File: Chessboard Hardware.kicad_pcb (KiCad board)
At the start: 2 copper layers, 200 x 200 mm, 86 parts, among them J1 Conn_01x04_Pin

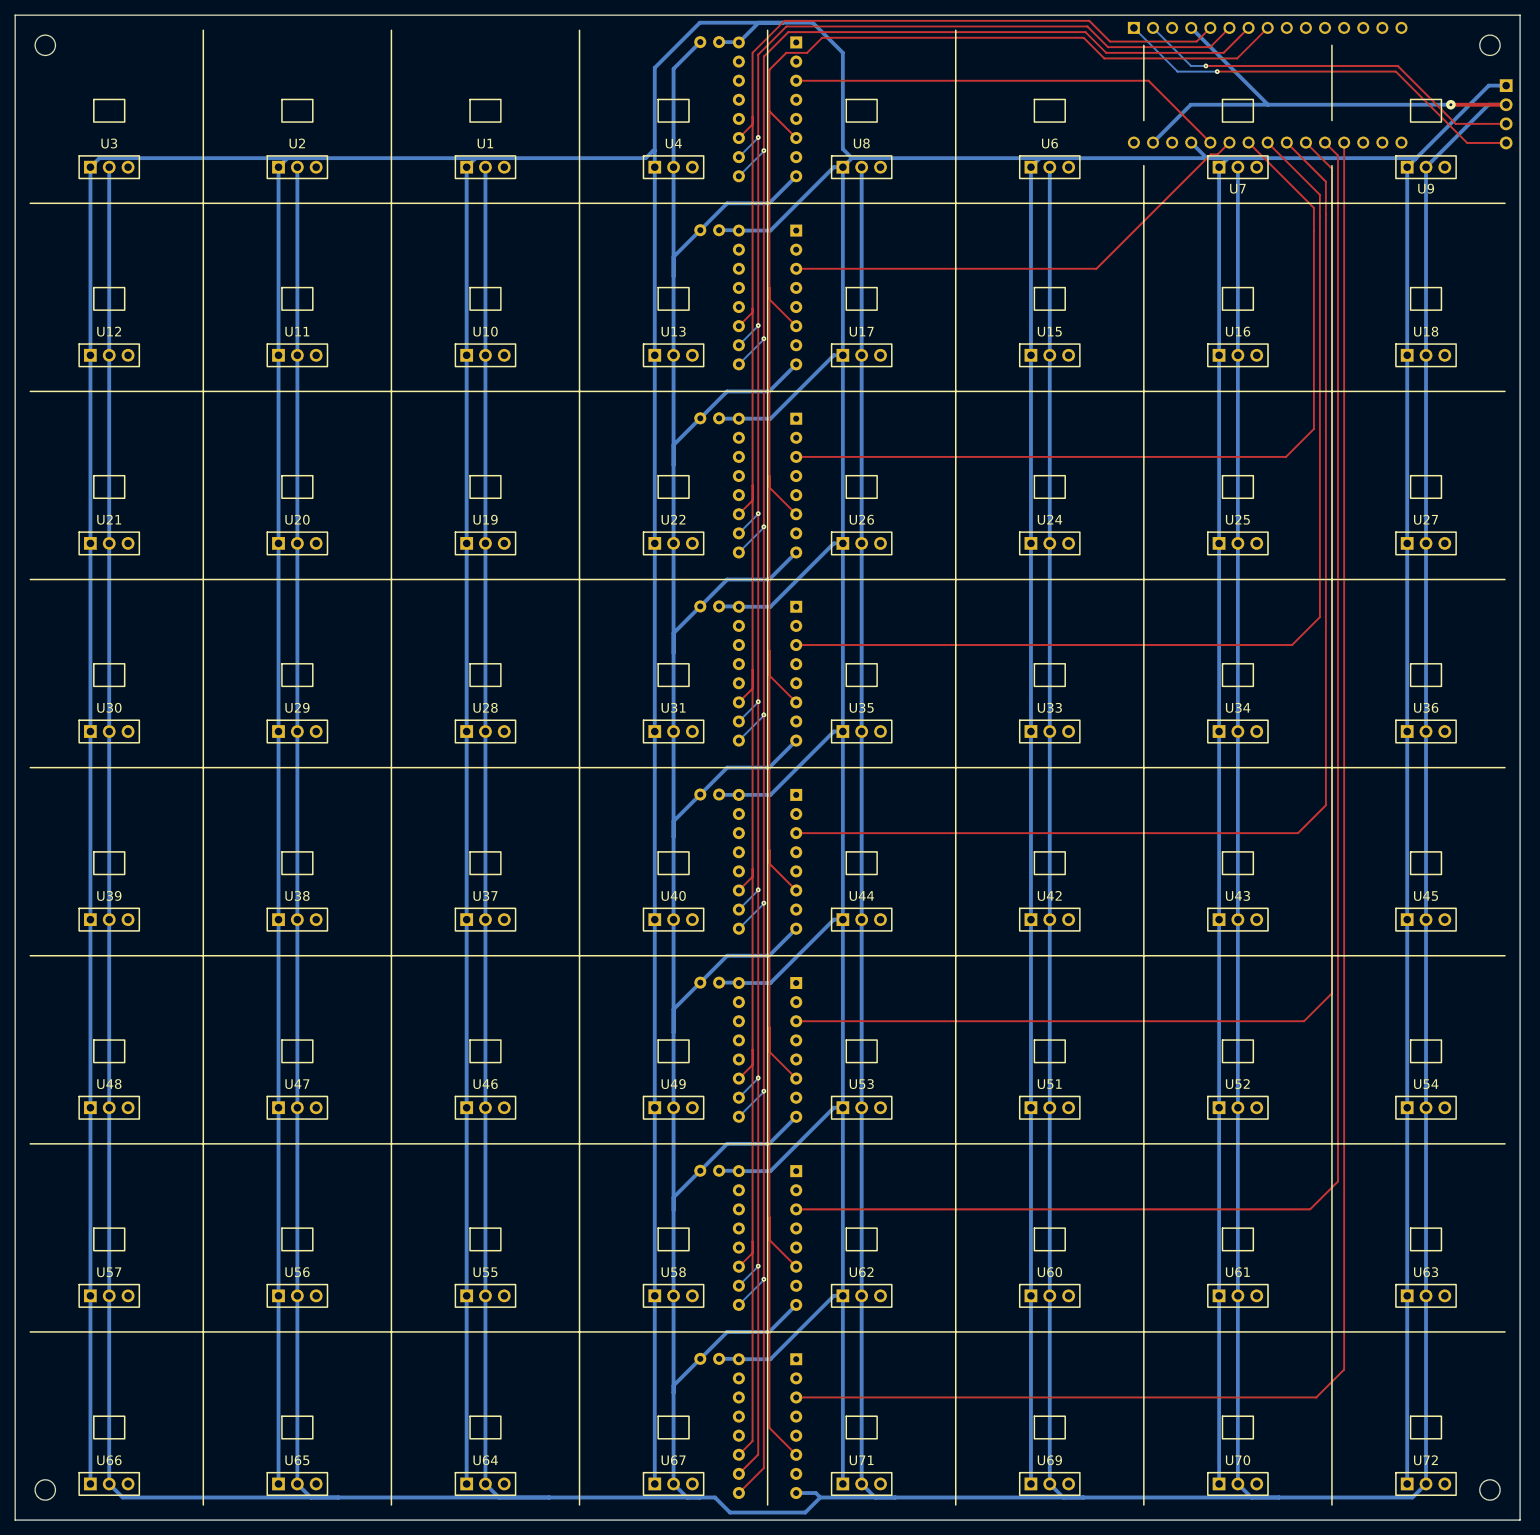
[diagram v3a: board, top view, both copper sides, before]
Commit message: Route left side linear halls
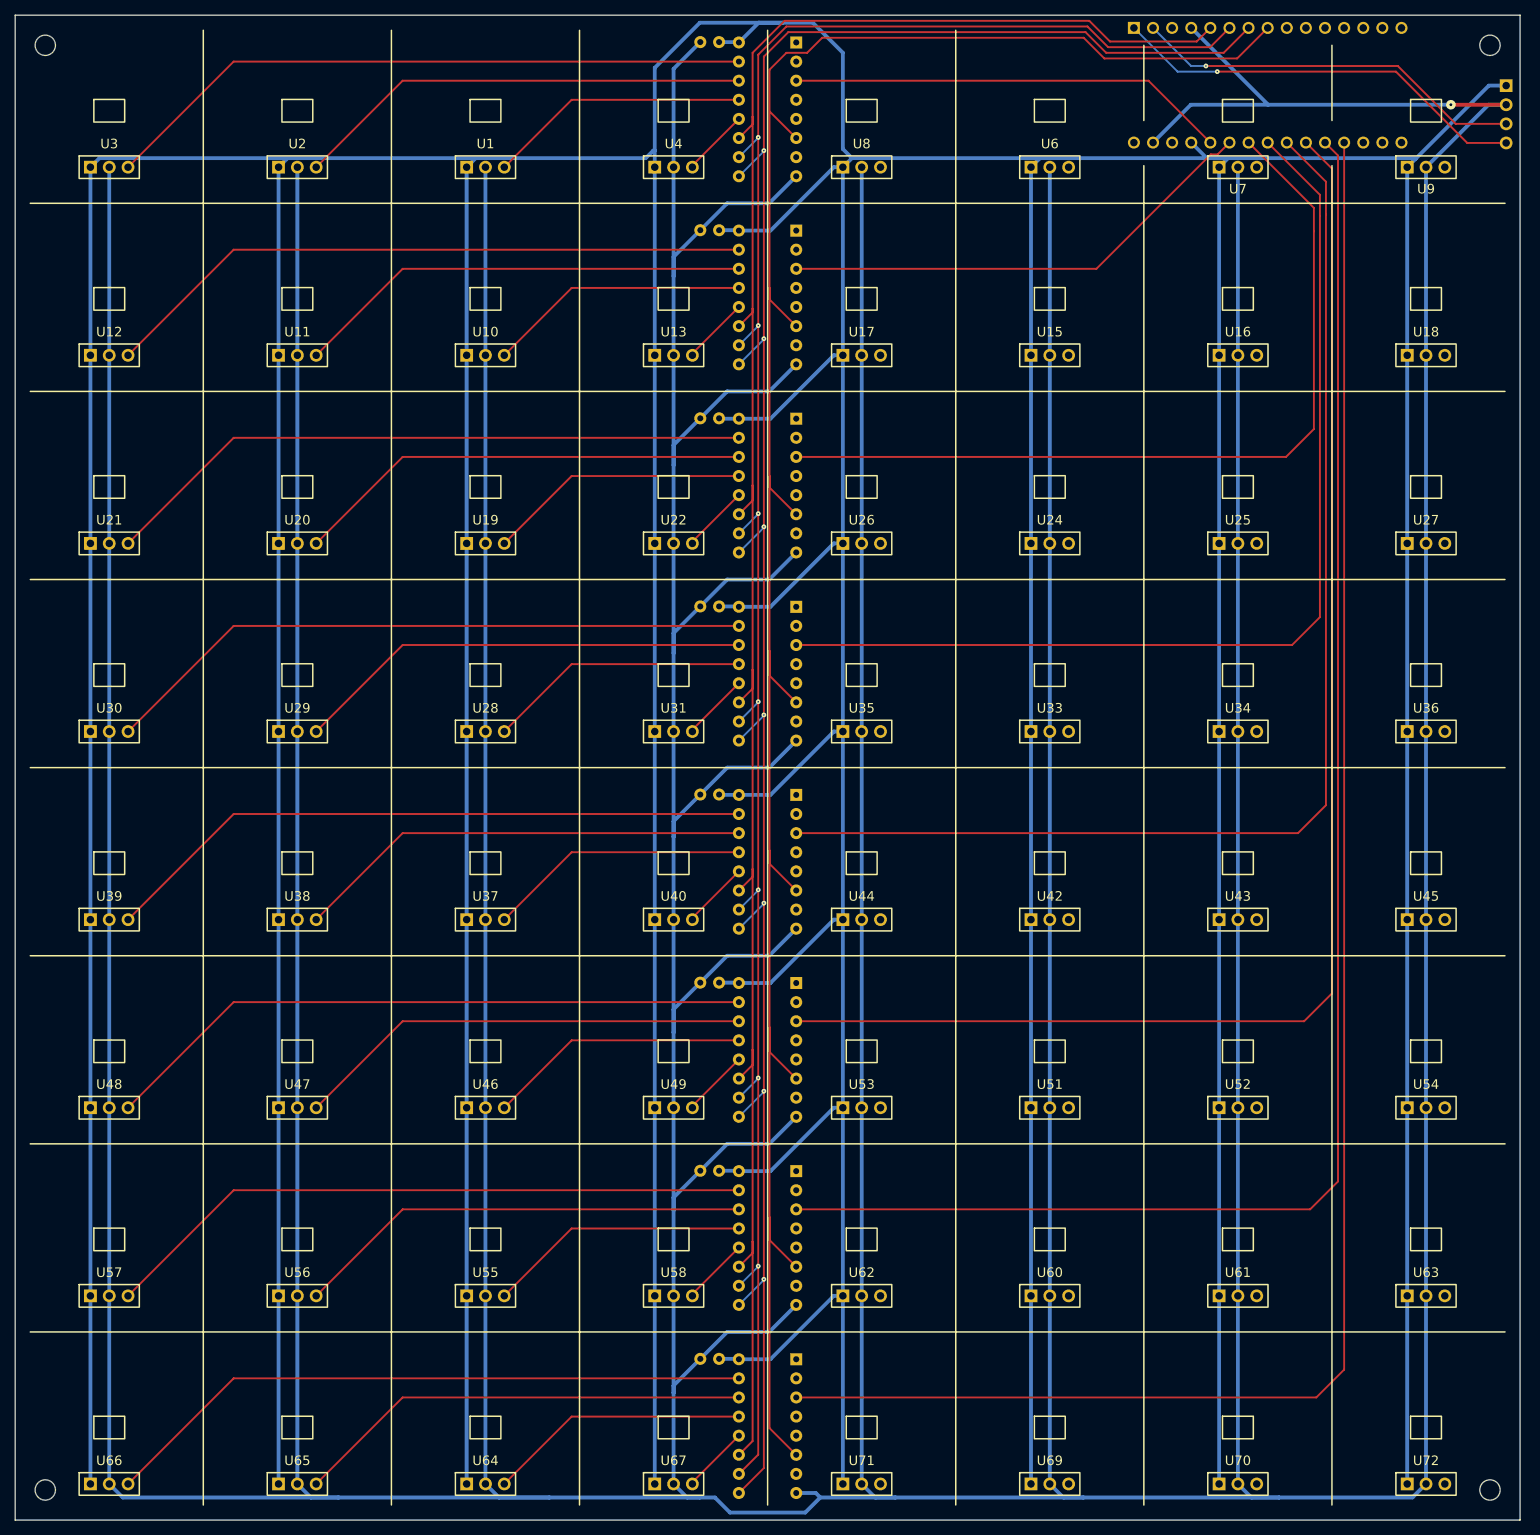
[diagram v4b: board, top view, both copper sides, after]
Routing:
- net Net-(U66-SIG): track 0.00 -> 87.0 mm
- net Net-(U57-SIG): track 0.00 -> 87.0 mm
- net Net-(U48-SIG): track 0.00 -> 87.0 mm
- net Net-(U39-SIG): track 0.00 -> 87.0 mm
- net Net-(U30-SIG): track 0.00 -> 87.0 mm
- net Net-(U3-SIG): track 0.00 -> 87.0 mm
- net Net-(U21-SIG): track 0.00 -> 87.0 mm
- net Net-(U12-SIG): track 0.00 -> 87.0 mm
- net Net-(U20-SIG): track 0.00 -> 60.9 mm
- net Net-(U2-SIG): track 0.00 -> 60.9 mm
- net Net-(U11-SIG): track 0.00 -> 60.9 mm
- net Net-(U65-SIG): track 0.00 -> 60.9 mm
- net Net-(U56-SIG): track 0.00 -> 60.9 mm
- net Net-(U47-SIG): track 0.00 -> 60.9 mm
- net Net-(U38-SIG): track 0.00 -> 60.9 mm
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
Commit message: Finish routing linear halls
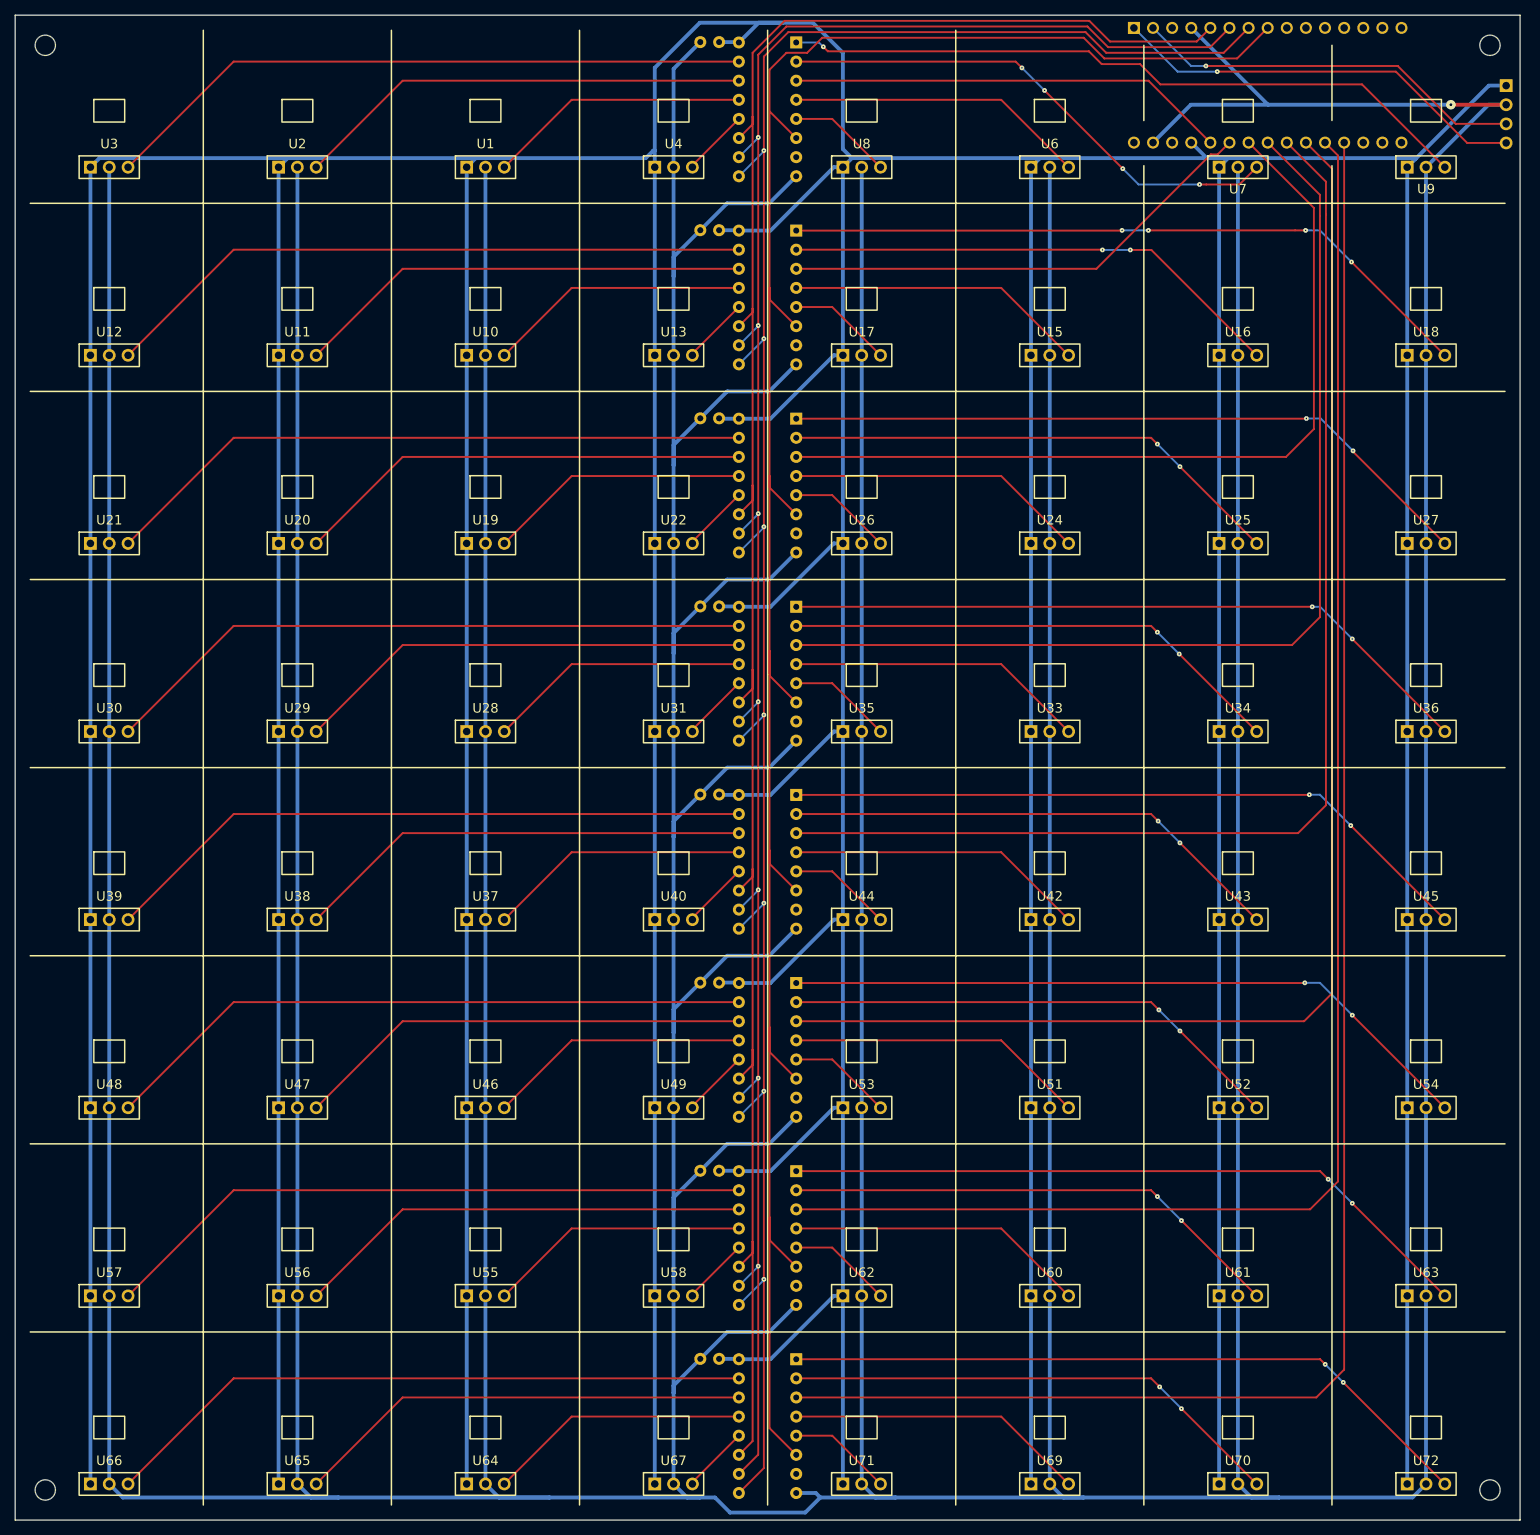
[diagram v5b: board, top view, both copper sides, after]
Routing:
- net Net-(U23-Y4): track 0.00 -> 93.1 mm, vias 0 -> 2
- net Net-(U32-Y4): track 0.00 -> 93.1 mm, vias 0 -> 2
- net Net-(U14-Y4): track 0.00 -> 93.1 mm, vias 0 -> 4
- net Net-(U41-Y4): track 0.00 -> 93.1 mm, vias 0 -> 2
- net Net-(U50-Y4): track 0.00 -> 93.1 mm, vias 0 -> 2
- net Net-(U5-Y4): track 0.00 -> 93.1 mm, vias 0 -> 1
- net Net-(U68-Y4): track 0.00 -> 93.1 mm, vias 0 -> 2
- net Net-(U59-Y4): track 0.00 -> 93.1 mm, vias 0 -> 2
- net Net-(U5-Y6): track 0.00 -> 68.9 mm, vias 0 -> 4
- net Net-(U68-Y6): track 0.00 -> 67.0 mm, vias 0 -> 2
- net Net-(U59-Y6): track 0.00 -> 67.0 mm, vias 0 -> 2
- net Net-(U50-Y6): track 0.00 -> 67.0 mm, vias 0 -> 2
- net Net-(U41-Y6): track 0.00 -> 67.0 mm, vias 0 -> 2
- net Net-(U32-Y6): track 0.00 -> 67.0 mm, vias 0 -> 2
- net Net-(U23-Y6): track 0.00 -> 67.0 mm, vias 0 -> 2
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
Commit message: Finish test pad routing
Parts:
- added TP1: TestPoint, Connector_PinHeader_2.54mm:PinHeader_1x01_P2.54mm_Vertical, B.Cu at (240.0, 78.3)
- added TP10: TestPoint, Connector_PinHeader_2.54mm:PinHeader_1x01_P2.54mm_Vertical, B.Cu at (221.0, 137.0)
- added TP11: TestPoint, Connector_PinHeader_2.54mm:PinHeader_1x01_P2.54mm_Vertical, B.Cu at (221.0, 162.0)
- added TP12: TestPoint, Connector_PinHeader_2.54mm:PinHeader_1x01_P2.54mm_Vertical, B.Cu at (221.0, 187.0)
- added TP13: TestPoint, Connector_PinHeader_2.54mm:PinHeader_1x01_P2.54mm_Vertical, B.Cu at (221.0, 212.0)
- added TP14: TestPoint, Connector_PinHeader_2.54mm:PinHeader_1x01_P2.54mm_Vertical, B.Cu at (221.0, 237.0)
- added TP2: TestPoint, Connector_PinHeader_2.54mm:PinHeader_1x01_P2.54mm_Vertical, B.Cu at (240.0, 83.0)
- added TP3: TestPoint, Connector_PinHeader_2.54mm:PinHeader_1x01_P2.54mm_Vertical, B.Cu at (177.0, 65.0)
- added TP4: TestPoint, Connector_PinHeader_2.54mm:PinHeader_1x01_P2.54mm_Vertical, B.Cu at (173.0, 65.0)
- added TP5: TestPoint, Connector_PinHeader_2.54mm:PinHeader_1x01_P2.54mm_Vertical, B.Cu at (169.0, 65.0)
- added TP6: TestPoint, Connector_PinHeader_2.54mm:PinHeader_1x01_P2.54mm_Vertical, B.Cu at (181.0, 65.0)
- added TP7: TestPoint, Connector_PinHeader_2.54mm:PinHeader_1x01_P2.54mm_Vertical, B.Cu at (191.0, 57.0)
- added TP8: TestPoint, Connector_PinHeader_2.54mm:PinHeader_1x01_P2.54mm_Vertical, B.Cu at (196.0, 87.0)
- added TP9: TestPoint, Connector_PinHeader_2.54mm:PinHeader_1x01_P2.54mm_Vertical, B.Cu at (221.0, 112.0)
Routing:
- net /A: track 280.1 -> 306.8 mm, vias 0 -> 1
- net /INH: track 305.9 -> 324.7 mm, vias 0 -> 1
- net /B: track 281.8 -> 295.3 mm, vias 7 -> 8
- net /C: track 294.0 -> 306.8 mm, vias 7 -> 8
- net VCC: track 1793.3 -> 1803.5 mm
- net /COM5: track 187.2 -> 195.6 mm
- net /COM7: track 237.4 -> 244.8 mm
- net /COM6: track 212.3 -> 219.7 mm
- net /COM2: track 112.0 -> 119.4 mm
- net /COM1: track 64.5 -> 71.9 mm
- net /COM4: track 162.2 -> 169.5 mm
- net /COM3: track 137.1 -> 144.4 mm
- net GND: track 1874.6 -> 1878.6 mm
- net /COM0: track 58.4 -> 62.2 mm

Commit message: Ground plane
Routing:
- added copper zone on B.Cu, net GND
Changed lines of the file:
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@@
 		(net 100)
 	)
+	(zone
+		(net 12)
+		(net_name "GND")
+		(layer "B.Cu")
+		(hatch edge 0.5)
+		(connect_pads
+			(clearance 0.508)
+		)
+		(min_thickness 0.25)
+		(filled_areas_thickness no)
+		(fill yes
+			(thermal_gap 0.5)
+			(thermal_bridge_width 0.5)
+		)
+		(polygon
+			(pts
+				(xy 50 50) (xy 250 50.000001) (xy 250 250) (xy 50 250)
+			)
+		)
+	)
 )
